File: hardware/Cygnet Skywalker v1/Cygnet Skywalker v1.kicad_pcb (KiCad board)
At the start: 2 copper layers, 85 parts, among them J3 BM04B-SRSS-TB(LF)(SN), J4 BM04B-SRSS-TB(LF)(SN), J5 BM04B-SRSS-TB(LF)(SN), J7 Conn_01x02, J8 Hirose DF11 02x06, SW1 SW_Push, SW2 SW_Push, U1 RP2350_60QFN_C42411118, U11 RM-VT01-A Readout Module, U12 INA260, U13 INA260, U14 TLV1704, U15 REF200AU, U2 W25Q128JVS, U3 INA260, U5 MCP9808_MSOP, U6 VT01, U7 NCP1117-3.3_SOT223, Y1 ABM8-272-T3

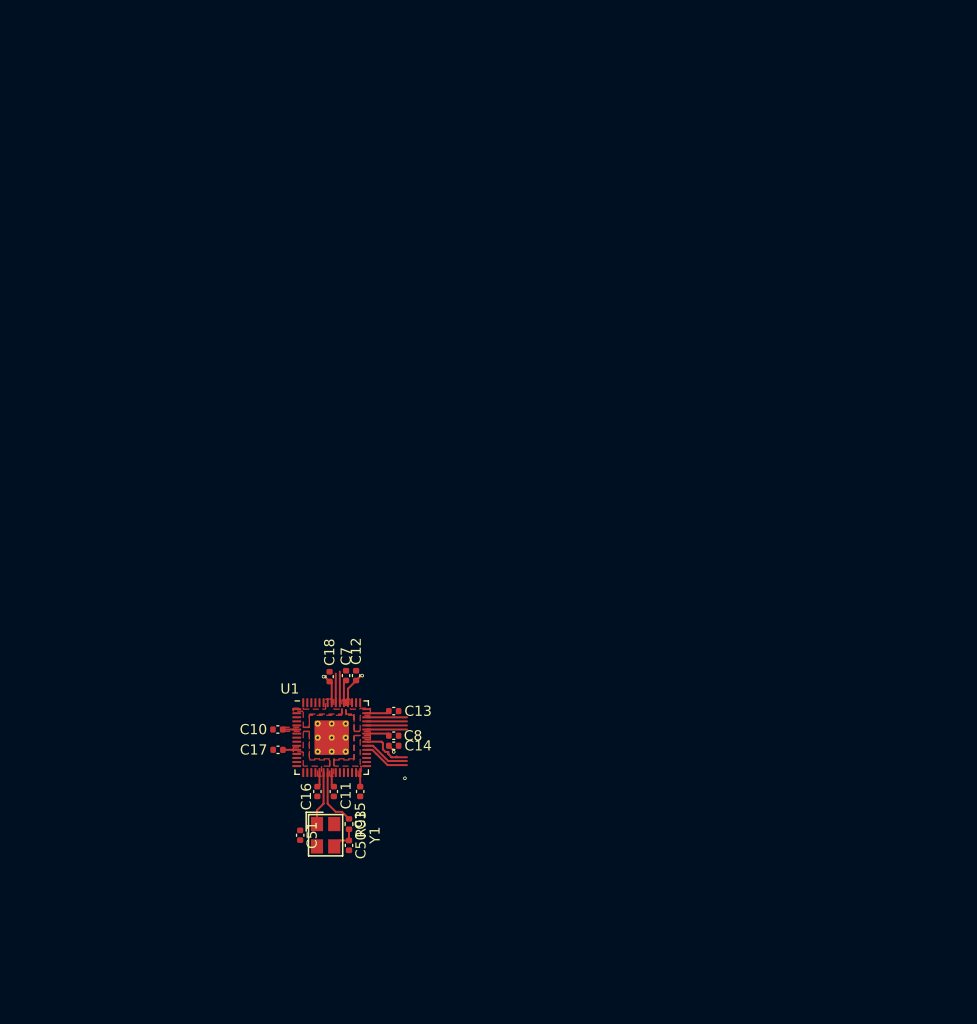
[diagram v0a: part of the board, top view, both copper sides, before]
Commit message: added edge cut for PCB
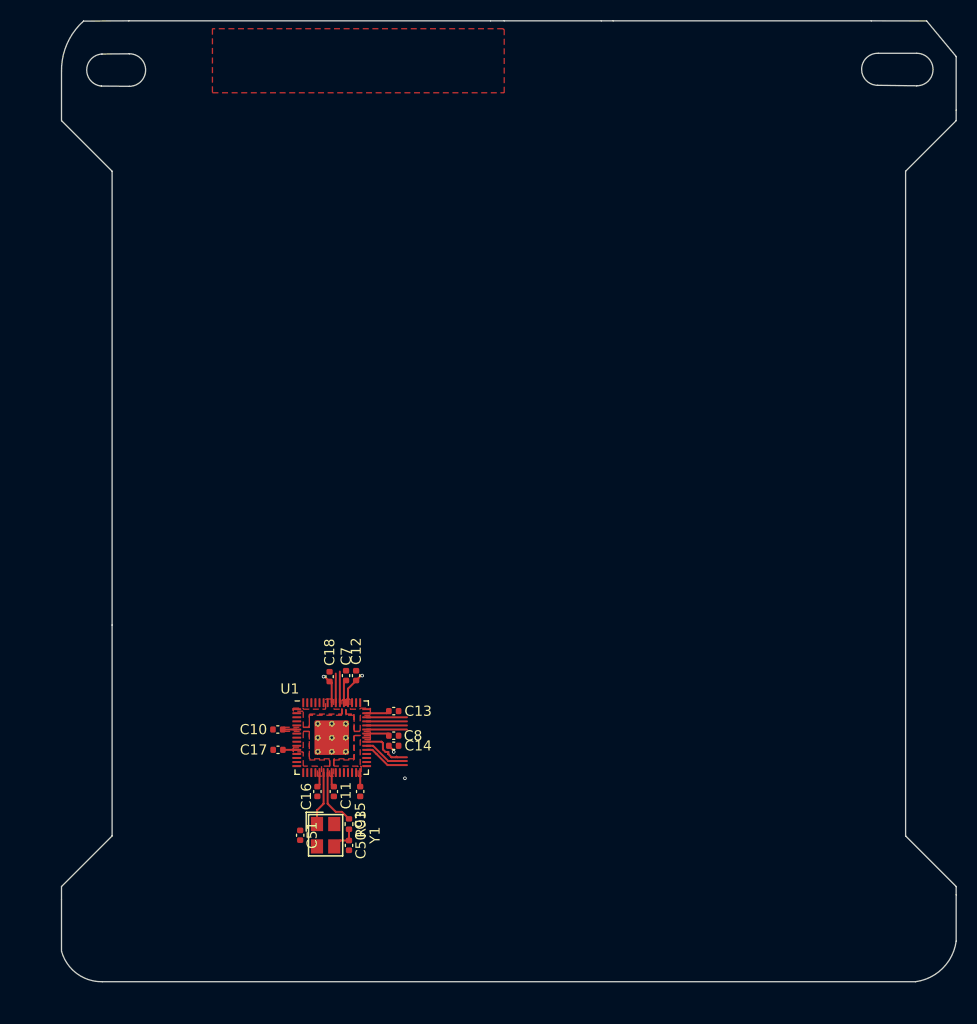
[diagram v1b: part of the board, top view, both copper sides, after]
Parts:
- added G***: LOGO, LOGO, F.Cu at (200.9, 46.0)
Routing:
- added copper zone on F.Cu, net PAYLOAD_PWR
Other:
- board outline added: 88 x 94.5 mm
- board text added: "${REFERENCE}"

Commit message: brought over changes made on max branch
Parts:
- removed C20: 100n, Capacitor_SMD:C_0402_1005Metric
- removed C21: 1u, Capacitor_SMD:C_0402_1005Metric
- removed C22, C23: 10u, Capacitor_SMD:C_0805_2012Metric
- removed C33: 10u, Capacitor_SMD:C_0402_1005Metric
- removed U15: REF200AU, Package_SO:SOIC-8_3.9x4.9mm_P1.27mm
- removed U7: NCP1117-3.3_SOT223, Package_TO_SOT_SMD:SOT-223-3_TabPin2
- added D14: NSR0320, Diode_SMD:D_SOD-323F, F.Cu at (139.1, 120.5)
- added U17: LM234Z-6, Package_TO_SOT_THT:TO-92_Inline, F.Cu at (139.0, 114.5)
- C39: value 100n -> 1u
- moved G*** 26.5 mm to (201.1, 72.4)
- moved U11 25.9 mm to (129.0, 61.3)
- moved C13 13.3 mm to (213.4, 120.1)
- moved C14 13.3 mm to (213.4, 123.5)
- moved C17 13.3 mm to (202.0, 123.9)
- moved C18 13.3 mm to (207.1, 116.7)
- moved C7 13.3 mm to (208.7, 116.6)
- moved C8 13.3 mm to (213.4, 122.5)
- moved U1 13.3 mm to (207.3, 122.7)
- moved C50 13.3 mm to (209.0, 133.3)
- moved C51 13.3 mm to (204.2, 132.3)
- moved Y1 13.3 mm to (206.7, 132.3)
- moved C10 13.3 mm to (202.0, 121.9)
- moved C11 13.3 mm to (207.5, 128.0)
- moved C12 13.3 mm to (209.7, 116.6)
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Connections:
- R16 pad 1: /CubeSat's Best Friend/WDT-VIN -> +5V
- R30 pad 1: /CubeSat's Best Friend/WDT-VIN -> +5V
- R36 pad 2: /CubeSat's Best Friend/WDT-VIN -> +5V
- SW1 pad 2: /RP2350/QSPI_SS -> Net-(R26-Pad2)
- U14 pad 3: /CubeSat's Best Friend/WDT-VIN -> +5V
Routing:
- added copper zone on F.Cu, net (none)
- removed copper zone on F.Cu, net PAYLOAD_PWR
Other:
- board text removed: "${REFERENCE}"

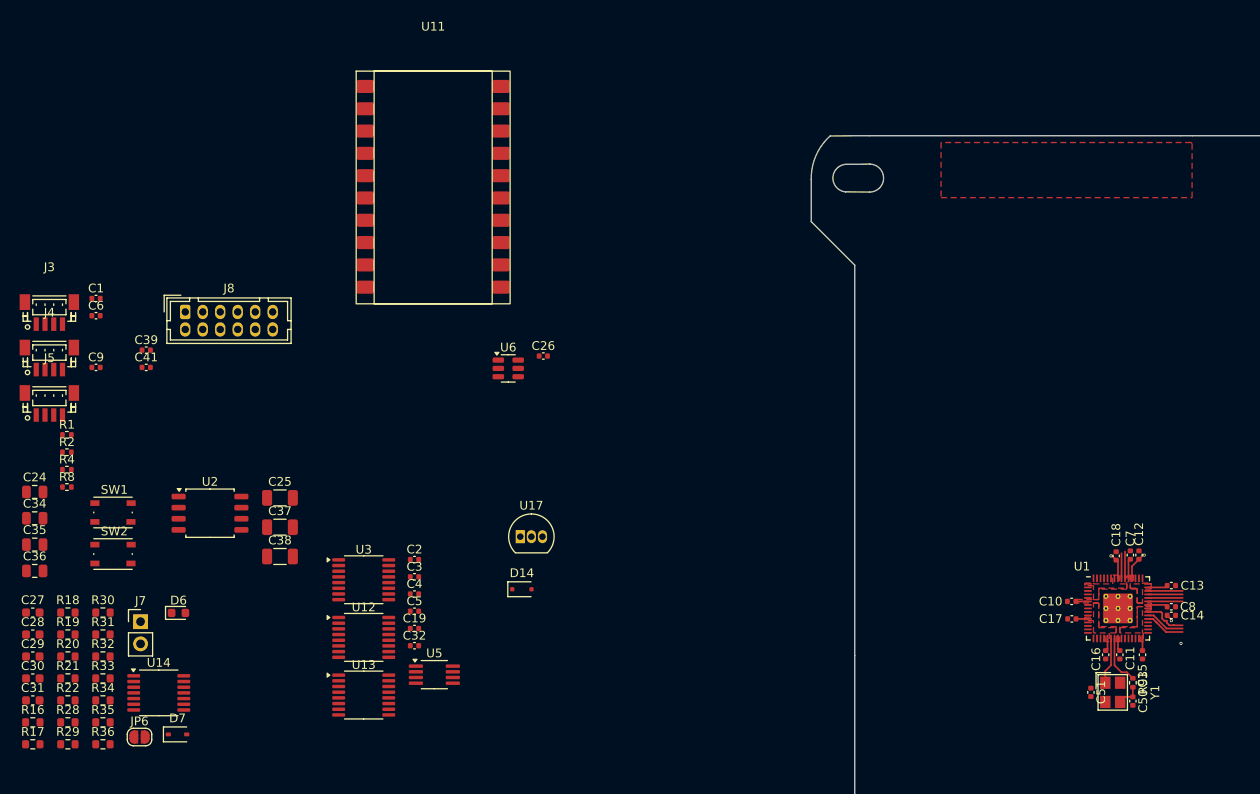
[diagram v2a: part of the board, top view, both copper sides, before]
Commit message: schematic changes
-replaced custom circuitry with radfet readout modules
-cleaned up sensor schematic page
-changed temp sensor
-added more missing footprints
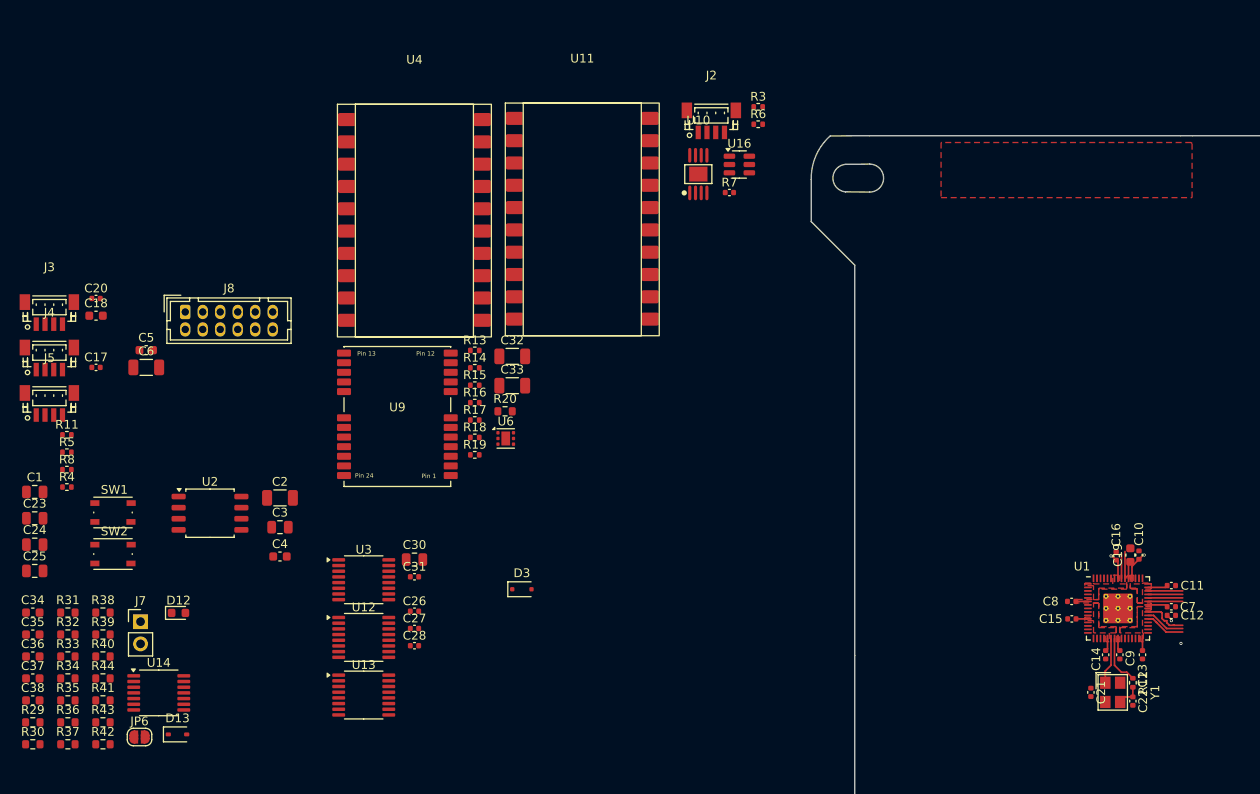
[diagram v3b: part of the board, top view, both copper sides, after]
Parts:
- removed the C26 at (141.6, 93.8)
- removed the C4 at (126.9, 121.1)
- removed U17: LM234Z-6, Package_TO_SOT_THT:TO-92_Inline
- removed U5: MCP9808_MSOP, Package_SO:MSOP-8_3x3mm_P0.65mm
- added C32: 10u, Capacitor_SMD:C_1206_3216Metric, F.Cu at (138.0, 93.9)
- added C33: 10u, Capacitor_SMD:C_1206_3216Metric, F.Cu at (138.0, 97.2)
- added J2: BM04B-SRSS-TB(LF)(SN), Skywalkerfeet:BM04B-SRSS-TB(LF)(SN), F.Cu at (160.8, 67.0)
- added R13: 1k, Resistor_SMD:R_0402_1005Metric, F.Cu at (133.8, 93.2)
- added R14: 10k, Resistor_SMD:R_0402_1005Metric, F.Cu at (133.8, 95.2)
- added R15: 10k, Resistor_SMD:R_0402_1005Metric, F.Cu at (133.8, 97.2)
- added R16: 10k, Resistor_SMD:R_0402_1005Metric, F.Cu at (133.8, 99.2)
- added R17: 10k, Resistor_SMD:R_0402_1005Metric, F.Cu at (133.8, 101.2)
- added R18: 10k, Resistor_SMD:R_0402_1005Metric, F.Cu at (133.8, 103.2)
- added R19: 6.8k, Resistor_SMD:R_0402_1005Metric, F.Cu at (133.8, 105.1)
- added R20: 20k, Resistor_SMD:R_0603_1608Metric, F.Cu at (137.2, 100.2)
- added R3: 33, Resistor_SMD:R_0402_1005Metric, F.Cu at (166.2, 65.4)
- added R6: 1k, Resistor_SMD:R_0402_1005Metric, F.Cu at (166.2, 67.3)
- added R7: 10k, Capacitor_SMD:C_0402_1005Metric, F.Cu at (162.9, 75.2)
- added U10: TLV76733DGNR, Skywalkerfeet:TLV76733DGNR, F.Cu at (159.3, 73.0)
- added U16: TLV61048, Package_TO_SOT_SMD:SOT-23-6, F.Cu at (164.0, 72.0)
- added U4: RM-VT01-A Readout Module, Skywalkerfeet:RM-VT01-A, F.Cu at (126.9, 65.1)
- added U9: Skytraq Orion B16 GPS, Skywalkerfeet:Skytraq Orion B16 GPS, F.Cu at (124.9, 99.7)
- C18: renamed from C6; footprint Capacitor_SMD:C_0402_1005Metric -> Capacitor_SMD:C_0603_1608Metric
- C19: renamed from C7; footprint Capacitor_SMD:C_0402_1005Metric -> Capacitor_SMD:C_0603_1608Metric
- C3: renamed from C37; footprint Capacitor_SMD:C_1206_3216Metric -> Capacitor_SMD:C_0805_2012Metric
- C30: renamed from C2; footprint Capacitor_SMD:C_0402_1005Metric -> Capacitor_SMD:C_0805_2012Metric
- C4: renamed from C38; footprint Capacitor_SMD:C_1206_3216Metric -> Capacitor_SMD:C_0603_1608Metric
- C5: renamed from C39; footprint Capacitor_SMD:C_0402_1005Metric -> Capacitor_SMD:C_0603_1608Metric
- C6: renamed from C41; footprint Capacitor_SMD:C_0402_1005Metric -> Capacitor_SMD:C_1206_3216Metric
- U6: value VT01 -> TMP117xxDRV; footprint Package_TO_SOT_SMD:SOT-23-6 -> Package_SON:WSON-6-1EP_2x2mm_P0.65mm_EP1x1.6mm
- moved U11 17.4 mm to (146.1, 65.0)
- moved U6 8.02 mm to (137.3, 103.3)
- renumbered C24 to C1, C12 to C10, C13 to C11, C14 to C12, C15 to C13, C16 to C14, C17 to C15, C18 to C16, C9 to C17, C25 to C2, C1 to C20, C51 to C21, C50 to C22, C34 to C23, C35 to C24, C36 to C25, C5 to C26, C19 to C27, C32 to C28, C3 to C31, C27 to C34, C28 to C35, C29 to C36, C30 to C37, C31 to C38, C8 to C7, C10 to C8, C11 to C9, D6 to D12, D7 to D13, D14 to D3, R1 to R11, R93 to R12, R16 to R29, R17 to R30, R18 to R31, R19 to R32, R20 to R33, R21 to R34, R22 to R35, R28 to R36, R29 to R37, R30 to R38, R31 to R39, R8 to R4, R32 to R40, R34 to R41, R36 to R42, R35 to R43, R33 to R44, R2 to R5, R4 to R8
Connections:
- U1 pad 10: RADFET Sense CTRL -> unconnected-(U1-GPIO7-Pad10)
- U1 pad 12: RADFET Read CTRL -> unconnected-(U1-GPIO8-Pad12)
- U1 pad 8: RADFET R2 CTRL -> unconnected-(U1-GPIO5-Pad8)
- U1 pad 9: RADFET R1 CTRL -> unconnected-(U1-GPIO6-Pad9)
- U12 pad 5: unconnected-(U12-A0-Pad5) -> SDA1
- U3 pad 4: unconnected-(U3-A1-Pad4) -> GND
- U3 pad 5: unconnected-(U3-A0-Pad5) -> +3.3V
- U6 pad 1: Net-(R27-Pad2) -> SCL1
- U6 pad 2: RADFET Vo -> GND
- U6 pad 3: Net-(Q4-D) -> unconnected-(U6-ALERT-Pad3)
- U6 pad 4: Net-(Q5-D) -> GND
- U6 pad 5: Net-(Q4-D) -> +3.3V
- U6 pad 6: Net-(Q5-D) -> SDA1

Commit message: carried over cygnet skywalker v1 from max-layout
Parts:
- removed the G*** at (201.1, 72.4)
- removed JP6: SolderJumper_2_Open, Jumper:SolderJumper-2_P1.3mm_Open_RoundedPad1.0x1.5mm
- removed R42, R44: 100k, Resistor_SMD:R_0603_1608Metric
- removed R43: 4.7M, Resistor_SMD:R_0603_1608Metric
- removed U16: TLV61048, Package_TO_SOT_SMD:SOT-23-6
- added C29: 100n, Capacitor_SMD:C_0402_1005Metric, F.Cu at (223.2, 96.2)
- added C39: 10uF, Capacitor_SMD:C_0603_1608Metric, F.Cu at (250.7, 91.5)
- added C40: 10uF, Capacitor_SMD:C_0603_1608Metric, F.Cu at (249.2, 91.5)
- added C41: 10uF, Capacitor_SMD:C_0603_1608Metric, F.Cu at (244.0, 86.0)
- added C42: 10uF, Capacitor_SMD:C_0603_1608Metric, F.Cu at (244.0, 87.5)
- added C43: 10uF, Capacitor_SMD:C_0603_1608Metric, F.Cu at (252.8, 83.0)
- added D1: RED, LED_SMD:LED_0603_1608Metric, F.Cu at (199.6, 79.6)
- added D10: YELLOW, LED_SMD:LED_0603_1608Metric, F.Cu at (214.9, 157.4)
- added D11: B120AF-13, Skywalkerfeet:B120AF-13, F.Cu at (209.7, 90.6)
- added D2: B120AF-13, Skywalkerfeet:B120AF-13, F.Cu at (194.8, 96.0)
- added D4: BLUE, LED_SMD:LED_0603_1608Metric, F.Cu at (193.4, 79.5)
- added D5: WHITE, LED_SMD:LED_0603_1608Metric, F.Cu at (190.1, 79.6)
- added D6: NSR0320, Diode_SMD:D_SOD-323F, F.Cu at (204.3, 114.7)
- added D7: RED, LED_SMD:LED_0603_1608Metric, F.Cu at (196.2, 137.4)
- added D8: RED, LED_SMD:LED_0603_1608Metric, F.Cu at (193.0, 137.4)
- added D9: YELLOW, LED_SMD:LED_0603_1608Metric, F.Cu at (218.1, 157.5)
- added G***: LOGO, LOGO, F.Cu at (208.0, 70.6)
- added G***: LOGO, 1my_footprints:cadence_cygnet_logo_placeholder, F.Cu at (227.7, 70.9)
- added G***: LOGO, LOGO, B.Cu at (249.4, 111.7)
- added H1: MountingHole, MountingHole:MountingHole_3.2mm_M3_DIN965_Pad, F.Cu at (184.3, 156.9)
- added H2: MountingHole, MountingHole:MountingHole_3.2mm_M3_DIN965_Pad, F.Cu at (264.3, 156.9)
- added J1: USB_B_Micro, Skywalkerfeet:MICRO-USB-SMD_10118194-0001LF, F.Cu at (188.3, 99.8)
- added J10: BM04B-SRSS-TB(LF)(SN), Skywalkerfeet:BM04B-SRSS-TB(LF)(SN), F.Cu at (203.2, 136.4)
- added J11: Conn_Coaxial, Skywalkerfeet:SMA-TH_132134, F.Cu at (192.0, 144.1)
- added J12: Conn_01x02, Connector_PinHeader_2.54mm:PinHeader_1x02_P2.54mm_Vertical, F.Cu at (240.7, 91.8)
- added J6: BM04B-SRSS-TB(LF)(SN), Skywalkerfeet:BM04B-SRSS-TB(LF)(SN), F.Cu at (208.1, 104.0)
- added J9: BM04B-SRSS-TB(LF)(SN), Skywalkerfeet:BM04B-SRSS-TB(LF)(SN), F.Cu at (234.2, 148.7)
- added JP1: SolderJumper_2_Open, Jumper:SolderJumper-2_P1.3mm_Open_RoundedPad1.0x1.5mm, F.Cu at (242.8, 79.9)
- added L1: 3.3u, Skywalkerfeet:L_pol_2016, F.Cu at (221.9, 113.9)
- added L2: 2.2uH, Inductor_SMD:L_Coilcraft_XxL4020, F.Cu at (194.3, 104.8)
- added L3: 4.7uH, Skywalkerfeet:SWPA5040S4R7NT, F.Cu at (207.0, 84.5)
- added R1: 10k, Resistor_SMD:R_0402_1005Metric, F.Cu at (205.4, 108.8)
- added R10: 33, Resistor_SMD:R_0402_1005Metric, F.Cu at (224.3, 113.6)
- added R2: 1k, Resistor_SMD:R_0402_1005Metric, F.Cu at (221.7, 129.0)
- added R21: 1.5M, Resistor_SMD:R_0603_1608Metric, F.Cu at (214.0, 86.2)
- added R22: 107k, Resistor_SMD:R_0603_1608Metric, F.Cu at (214.0, 83.2)
- added R23: 4.7k, Resistor_SMD:R_0402_1005Metric, F.Cu at (227.7, 123.5)
- added R24: 4.7k, Resistor_SMD:R_0402_1005Metric, F.Cu at (229.2, 125.0)
- added R25: 10k, Resistor_SMD:R_0603_1608Metric, F.Cu at (252.2, 80.3)
- added R26: 10k, Resistor_SMD:R_0603_1608Metric, F.Cu at (252.8, 84.5)
- added R27: 10k, Resistor_SMD:R_0603_1608Metric, F.Cu at (252.8, 89.0)
- added R28: 3.0k, Resistor_SMD:R_0603_1608Metric, F.Cu at (252.8, 87.5)
- added R9: 1k, Resistor_SMD:R_0402_1005Metric, F.Cu at (206.5, 116.5)
- added TP1: 3.3V Testpoint, Skywalkerfeet:Keystone5001_Testpoint, F.Cu at (203.9, 77.8)
- added TP10: GND, Skywalkerfeet:Keystone5001_Testpoint, F.Cu at (227.4, 93.9)
- added TP2: Module1 Vo, Skywalkerfeet:Keystone5001_Testpoint, F.Cu at (234.6, 121.0)
- added TP3: 5V Testpoint, Skywalkerfeet:Keystone5001_Testpoint, F.Cu at (211.5, 77.8)
- added TP4: Module2 Vo, Skywalkerfeet:Keystone5001_Testpoint, F.Cu at (231.8, 116.5)
- added TP5: 12V Testpoint, Skywalkerfeet:Keystone5001_Testpoint, F.Cu at (219.3, 77.9)
- added TP6: GPS 1PPS, Skywalkerfeet:Keystone5001_Testpoint, F.Cu at (211.1, 139.7)
- added TP7: 7V Testpoint, Skywalkerfeet:Keystone5001_Testpoint, F.Cu at (226.5, 78.0)
- added TP8: GND, Skywalkerfeet:Keystone5001_Testpoint, F.Cu at (227.4, 85.0)
- added TP9: GND, Skywalkerfeet:Keystone5001_Testpoint, F.Cu at (227.3, 89.3)
- added U15: TLV1704, Package_SO:TSSOP-14_4.4x5mm_P0.65mm, F.Cu at (248.4, 85.8)
- added U5: TLV61048, Package_TO_SOT_SMD:SOT-23-6, F.Cu at (211.5, 84.3)
- added U7: INA260, Package_SO:TSSOP-16_4.4x5mm_P0.65mm, F.Cu at (202.0, 91.9)
- added U8: INA260, Package_SO:TSSOP-16_4.4x5mm_P0.65mm, F.Cu at (195.4, 127.2)
- C1: value 10u -> 15p; footprint Capacitor_SMD:C_0805_2012Metric -> Capacitor_SMD:C_0402_1005Metric
- C10, C11: value 100n -> 4.7u
- C12: value 100n -> 3.3nF; footprint Capacitor_SMD:C_0402_1005Metric -> Capacitor_SMD:C_0603_1608Metric
- C14: value 100n -> 22u; footprint Capacitor_SMD:C_0402_1005Metric -> Capacitor_SMD:C_1206_3216Metric
- C16, C7: value 100n -> 1u; footprint Capacitor_SMD:C_0402_1005Metric -> Capacitor_SMD:C_0603_1608Metric
- C17, C8: value 4.7u -> 100n
- C18, C19: value 4.7u -> 100n; footprint Capacitor_SMD:C_0603_1608Metric -> Capacitor_SMD:C_0402_1005Metric
- C2: value 22u -> 15p; footprint Capacitor_SMD:C_1206_3216Metric -> Capacitor_SMD:C_0402_1005Metric
- C21: value 15p -> 100n
- C22: value 15p -> 10u; footprint Capacitor_SMD:C_0402_1005Metric -> Capacitor_SMD:C_1206_3216Metric
- C23, C30: value 10u -> 100n; footprint Capacitor_SMD:C_0805_2012Metric -> Capacitor_SMD:C_0402_1005Metric
- C26, C27, C28, C9: value 100n -> 10u; footprint Capacitor_SMD:C_0402_1005Metric -> Capacitor_SMD:C_0805_2012Metric
- C3: value 2.2u -> 1u; footprint Capacitor_SMD:C_0805_2012Metric -> Capacitor_SMD:C_0603_1608Metric
- C33: value 10u -> 100n; footprint Capacitor_SMD:C_1206_3216Metric -> Capacitor_SMD:C_0402_1005Metric
- C34, C37: value 10uF -> 100n; footprint Capacitor_SMD:C_0603_1608Metric -> Capacitor_SMD:C_0402_1005Metric
- C35: value 10uF -> 10u; footprint Capacitor_SMD:C_0603_1608Metric -> Capacitor_SMD:C_1206_3216Metric
- C36: value 10uF -> 10u; footprint Capacitor_SMD:C_0603_1608Metric -> Capacitor_SMD:C_0805_2012Metric
- C38: value 10uF -> 2.7n
- C4: value 1u -> 100n; footprint Capacitor_SMD:C_0603_1608Metric -> Capacitor_SMD:C_0402_1005Metric
- C5: value 1u -> 4.7u; footprint Capacitor_SMD:C_0603_1608Metric -> Capacitor_SMD:C_0402_1005Metric
- C6: value 10u -> 4.7u; footprint Capacitor_SMD:C_1206_3216Metric -> Capacitor_SMD:C_0402_1005Metric
- D3: value NSR0320 -> GREEN; footprint Diode_SMD:D_SOD-323F -> LED_SMD:LED_0603_1608Metric
- J2, J4: value BM04B-SRSS-TB(LF)(SN) -> Hirose DF11 02x06; footprint Skywalkerfeet:BM04B-SRSS-TB(LF)(SN) -> Connector_Hirose:Hirose_DF11-12DP-2DSA_2x06_P2.00mm_Vertical
- J3: value BM04B-SRSS-TB(LF)(SN) -> SWD Port; footprint Skywalkerfeet:BM04B-SRSS-TB(LF)(SN) -> Connector_PinHeader_1.27mm:PinHeader_2x02_P1.27mm_Vertical
- J7: value Conn_01x02 -> BM04B-SRSS-TB(LF)(SN); footprint Connector_PinHeader_2.54mm:PinHeader_1x02_P2.54mm_Vertical -> Skywalkerfeet:BM04B-SRSS-TB(LF)(SN)
- J8: value Hirose DF11 02x06 -> BM04B-SRSS-TB(LF)(SN); footprint Connector_Hirose:Hirose_DF11-12DP-2DSA_2x06_P2.00mm_Vertical -> Skywalkerfeet:BM04B-SRSS-TB(LF)(SN)
- R11: footprint Resistor_SMD:R_0402_1005Metric -> Capacitor_SMD:C_0402_1005Metric
- R12: value 1k -> 10k; footprint Resistor_SMD:R_0402_1005Metric -> Resistor_SMD:R_0603_1608Metric
- R13: value 1k -> 10k
- R14, R15, R16: footprint Resistor_SMD:R_0402_1005Metric -> Resistor_SMD:R_0603_1608Metric
- R17, R18: value 10k -> 27
- R19: value 6.8k -> 4.7k
- R20: value 20k -> 4.7k; footprint Resistor_SMD:R_0603_1608Metric -> Resistor_SMD:R_0402_1005Metric
- R29, R30: value 10k -> 3.0k
- R3: value 33 -> 220; footprint Resistor_SMD:R_0402_1005Metric -> Resistor_SMD:R_0603_1608Metric
- R32: value 3.0k -> 10k
- R33: value 3.0k -> 1k
- R34: value 3.0k -> 100k
- R35: value 10k -> 1k
- R36: value 10k -> 100k
- R37: value 1k -> 100k
- R39: value 1k -> 4.7M
- R4: value 27 -> 470; footprint Resistor_SMD:R_0402_1005Metric -> Resistor_SMD:R_0603_1608Metric
- R41: value 100k -> 4.7k; footprint Resistor_SMD:R_0603_1608Metric -> Resistor_SMD:R_0402_1005Metric
- R5: value 27 -> 10k
- R6: value 1k -> 1.47k; footprint Resistor_SMD:R_0402_1005Metric -> Resistor_SMD:R_0603_1608Metric
- R7: value 10k -> 1k; footprint Capacitor_SMD:C_0402_1005Metric -> Resistor_SMD:R_0402_1005Metric
- R8: value 1k -> 330; footprint Resistor_SMD:R_0402_1005Metric -> Resistor_SMD:R_0603_1608Metric
- SW1, SW2: footprint Button_Switch_SMD:SW_Push_1P1T_NO_Vertical_Wuerth_434133025816 -> Skywalkerfeet:KEY-SMD_KMR2XXGXXX
- U1: value RP2350_60QFN_C42411118 -> W25Q128JVS; footprint Skywalkerfeet:RP2350-QFN-60-1EP_7x7_P0.4mm_EP3.4x3.4mm_ThermalVias -> Package_SO:SOIC-8_5.3x5.3mm_P1.27mm
- U10: value TLV76733DGNR -> INA260; footprint Skywalkerfeet:TLV76733DGNR -> Package_SO:TSSOP-16_4.4x5mm_P0.65mm
- U12: value INA260 -> RM-VT01-A Readout Module; footprint Package_SO:TSSOP-16_4.4x5mm_P0.65mm -> Skywalkerfeet:RM-VT01-A
- U13: value INA260 -> Skytraq Orion B16 GPS; footprint Package_SO:TSSOP-16_4.4x5mm_P0.65mm -> Skywalkerfeet:Skytraq Orion B16 GPS
- U14: value TLV1704 -> TPS22992; footprint Package_SO:TSSOP-14_4.4x5mm_P0.65mm -> Skywalkerfeet:TPS22992
- U2: value W25Q128JVS -> TLV76733DGNR; footprint Package_SO:SOIC-8_5.3x5.3mm_P1.27mm -> Skywalkerfeet:TLV76733DGNR
- U3: value INA260 -> TPS62142; footprint Package_SO:TSSOP-16_4.4x5mm_P0.65mm -> Package_DFN_QFN:VQFN-16-1EP_3x3mm_P0.5mm_EP1.68x1.68mm_ThermalVias
- U4: value RM-VT01-A Readout Module -> RP2350_60QFN_C42411118; footprint Skywalkerfeet:RM-VT01-A -> Skywalkerfeet:RP2350-QFN-60-1EP_7x7_P0.4mm_EP3.4x3.4mm_ThermalVias
- U6: value TMP117xxDRV -> INA260; footprint Package_SON:WSON-6-1EP_2x2mm_P0.65mm_EP1x1.6mm -> Package_SO:TSSOP-16_4.4x5mm_P0.65mm
- U9: value Skytraq Orion B16 GPS -> TMP117xxDRV; footprint Skywalkerfeet:Skytraq Orion B16 GPS -> Package_SON:WSON-6-1EP_2x2mm_P0.65mm_EP1x1.6mm
- moved R29 176.7 mm to (252.8, 86.0)
- moved R30 175.3 mm to (252.2, 91.5), turned to 90 degrees
- moved R36 171.2 mm to (249.2, 80.3), turned to 90 degrees
- moved R39 165.8 mm to (250.7, 80.3), turned to -90 degrees
- moved R37 165.7 mm to (244.0, 84.5)
- moved R32 164.1 mm to (247.7, 91.5), turned to 90 degrees
- moved R34 163.7 mm to (246.2, 91.5), turned to -90 degrees
- moved R35 162.9 mm to (244.0, 89.0), turned to 180 degrees
- moved R38 162.2 mm to (247.7, 80.3), turned to 90 degrees
- moved R40 162.2 mm to (246.2, 80.3), turned to 90 degrees
- moved R33 161.7 mm to (244.7, 91.5), turned to -90 degrees
- moved R31 159.1 mm to (243.2, 91.5), turned to 90 degrees
- moved D12 157.0 mm to (253.7, 91.5), turned to 90 degrees
- moved C35 155.0 mm to (235.6, 97.0), turned to 180 degrees
- moved D13 154.0 mm to (243.9, 82.8), turned to 180 degrees
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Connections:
- C1 pad 1: PAYLOAD_BATT -> /RP2350/XIN
- C10 pad 1: +3.3V -> /RP2350/VREG_AVDD
- C11 pad 1: +3.3V -> +1V1
- C12 pad 1: +3.3V -> Net-(U3-SS/TR)
- C13 pad 1: +3.3V -> +1V1
- C14 pad 1: +3.3V -> PAYLOAD_PWR Test
- C17 pad 1: /RP2350/VREG_AVDD -> +3.3V
- C19 pad 1: +1V1 -> +3.3V
- C2 pad 1: +5V -> Net-(C2-Pad1)
- C21 pad 1: /RP2350/XIN -> +3.3V
- C22 pad 1: Net-(C22-Pad1) -> RADFET_PWR
- C23 pad 1: +5V -> +3.3V
- C3 pad 1: +3.3V -> +5V
- C33 pad 1: +12V -> +3.3V
- C34 pad 1: PET DOG -> +3.3V
- C34 pad 2: Net-(C34-Pad2) -> GND
- C35 pad 1: GND -> +12V
- C35 pad 2: Net-(U14B-+) -> GND
- C36 pad 1: GND -> GPS_PWR_SW_OUT
- C36 pad 2: WDT_DISABLE -> GND
- C37 pad 1: GND -> GPS_PWR_SW_OUT
- C37 pad 2: WDT_DISABLE -> GND
- C38 pad 1: GND -> Net-(U14-CT)
- C38 pad 2: Net-(U14D--) -> GND
- C4 pad 1: Net-(D1-K) -> +3.3V
- C5 pad 1: +5V -> +3.3V
- C6 pad 1: +12V -> +1V1
- C7 pad 1: +1V1 -> PAYLOAD_PWR Test
- C9 pad 1: +1V1 -> PAYLOAD_BATT_OUT
- D13 pad 1: Net-(U14D-+) -> Net-(U15D-+)
- D3 pad 1: Net-(D3-K) -> GND
- D3 pad 2: /RP2350/QSPI_SS -> Net-(D3-A)
- J2 pad 1: GND -> +3.3V
- J2 pad 2: RP2350 SWCLK -> GND
- J2 pad 3: RP2350 SWD -> +3.3V
- J3 pad 1: GND -> RP2350 Reset
- J3 pad 2: USB_D- -> RP2350 SWCLK
- J3 pad 3: USB_D+ -> GND
- J3 pad 4: GND -> RP2350 SWD
- J4 pad 1: GND -> PAYLOAD_PWR
- J4 pad 2: SCL0 -> PAYLOAD_PWR
- J4 pad 3: SDA0 -> GND
- J5 pad 2: SCL1 -> RP2350 SWD
- J5 pad 3: SDA1 -> RP2350 SWCLK
- J7 pad 1: WDT_DISABLE -> GND
- J7 pad 2: GND -> UART0 Tx
- J8 pad 1: PAYLOAD_PWR Test -> GND
- J8 pad 2: PAYLOAD_PWR Test -> SCL1
- J8 pad 3: GND -> SDA1
- R11 pad 2: /RP2350/QSPI_SS -> RP2350 Reset
- R12 pad 1: /RP2350/XOUT -> UART0 Tx
- R12 pad 2: Net-(C22-Pad1) -> Net-(D7-A)
- R13 pad 1: GPS Reset -> PAYLOAD_BATT_OUT
- R13 pad 2: GND -> DOG Bite
- R15 pad 1: UART0 Tx -> UART1 Tx
- R17 pad 1: UART1 Tx -> USB_D+
- R17 pad 2: Net-(D7-A) -> Net-(U4-USB_DP)
- R18 pad 1: +5V -> Net-(U4-USB_DM)
- R18 pad 2: Net-(D8-A) (its old number) -> USB_D-
- R19 pad 2: Net-(D9-A) (its old number) -> SCL0
- R20 pad 1: +12V -> +3.3V
- R20 pad 2: Net-(D10-A) (its old number) -> SDA0
- R29 pad 1: +5V -> /CubeSat's Best Friend/WDT-VP
- R29 pad 2: Net-(R29-Pad2) -> GND
- R3 pad 2: /RP2350/VREG_AVDD -> Net-(D1-A)
- R30 pad 1: Net-(R29-Pad2) -> PET DOG
- R30 pad 2: Net-(U14D--) -> Net-(D12-A)
- R31 pad 1: Net-(U14D--) -> Net-(C39-Pad2)
- R31 pad 2: Net-(U14B--) -> GND
- R32 pad 1: Net-(U14B--) -> Net-(C39-Pad2)
- R32 pad 2: /CubeSat's Best Friend/WDT-VP -> Net-(U15A--)
- R33 pad 1: /CubeSat's Best Friend/WDT-VP -> Net-(R33-Pad1)
- R33 pad 2: GND -> Net-(U15B-+)
- R34 pad 1: PET DOG -> +3.3V
- R34 pad 2: Net-(D12-A) -> Net-(U15B-+)
- R35 pad 1: Net-(C34-Pad2) -> Net-(R35-Pad1)
- R35 pad 2: GND -> WDT_DISABLE
- R36 pad 1: Net-(C34-Pad2) -> Net-(U15C-+)
- R36 pad 2: Net-(U14A--) -> Net-(R25-Pad2)
- R37 pad 1: Net-(R37-Pad1) -> Net-(D13-Pad2)
- R37 pad 2: Net-(U14B-+) -> WDT_DISABLE
- R38 pad 1: +5V -> Net-(U15C-+)
- R38 pad 2: Net-(U14B-+) -> Net-(U15D-+)
- R39 pad 1: Net-(R39-Pad1) -> Net-(U15D-+)
- R4 pad 1: USB D+ -> +5V
- R4 pad 2: Net-(U1-USB_DP) -> Net-(D3-A)
- R40 pad 1: Net-(U14C-+) -> Net-(U15D-+)
- R40 pad 2: Net-(R29-Pad2) -> +3.3V
- R41 pad 1: Net-(U14C-+) -> GPS Reset
- R41 pad 2: Net-(U14D-+) -> GND
- R5 pad 1: Net-(U1-USB_DM) -> +5V
- R5 pad 2: USB D- -> DOG Bite
- R6 pad 1: Net-(D3-K) -> +12V
- R6 pad 2: Net-(R6-Pad2) -> Net-(D4-A)
- R7 pad 1: +3.3V -> Net-(R7-Pad1)
- R7 pad 2: Net-(U1-RUN) -> GND
- R8 pad 1: Net-(R8-Pad1) -> PAYLOAD_BATT_OUT
- R8 pad 2: GND -> Net-(D5-A)
- SW1 pad 2: Net-(R6-Pad2) -> (no net)
- SW2 pad 1: Net-(R8-Pad1) -> Net-(R7-Pad1)
- SW2 pad 2: Net-(U1-RUN) -> (no net)
- U1 pad 1: +3.3V -> /RP2350/QSPI_SS
- U1 pad 2: UART0 Tx -> /RP2350/QSPI_SD1
- U1 pad 3: UART0 Rx -> /RP2350/QSPI_SD2
- U1 pad 4: Module R1 CTRL -> GND
- U1 pad 5: Module Enable CTRL -> /RP2350/QSPI_SD0
- U1 pad 6: +1V1 -> /RP2350/QSPI_SCLK
- U1 pad 7: Module R2 CTRL -> /RP2350/QSPI_SD3
- U1 pad 8: unconnected-(U1-GPIO5-Pad8) -> +3.3V
- U10 pad 3: unconnected-(U10-NC-Pad3) -> +3.3V
- U10 pad 4: GND -> SDA1
- U10 pad 5: DOG Bite -> SDA1
- U10 pad 8: Net-(D1-K) -> SDA1
- U10 pad 9: GND -> SCL1
- U11 pad 4: Module R2 CTRL -> Module1 R2 CTRL
- U11 pad 5: Module Enable CTRL -> Module1 Enable CTRL
- U11 pad 6: Module R1 CTRL -> Module1 R1 CTRL
- U11 pad 9: Module Vo -> Module1 Vo
- U12 pad 1: PAYLOAD_BATT Test -> +12V
- U12 pad 10: +3.3V -> (no net)
- U12 pad 11: GND -> (no net)
- U12 pad 12: PAYLOAD_BATT Test -> (no net)
- U12 pad 13: unconnected-(U12-NC-Pad13) -> (no net)
- U12 pad 14: PAYLOAD_BATT -> (no net)
- U12 pad 15: PAYLOAD_BATT -> (no net)
- U12 pad 16: PAYLOAD_BATT -> (no net)
- U12 pad 2: PAYLOAD_BATT Test -> GND
- U12 pad 3: PAYLOAD_BATT Test -> GND
- U12 pad 4: GND -> Module2 R2 CTRL
- U12 pad 5: SDA1 -> Module2 Enable CTRL
- U12 pad 6: GND -> Module2 R1 CTRL
- U12 pad 7: unconnected-(U12-ALERT-Pad7) -> (no net)
- U12 pad 8: SDA1 -> (no net)
- U12 pad 9: SCL1 -> Module2 Vo
- U13 pad 1: USB PWR Monitor -> unconnected-(U13-BOOT_SEL-Pad1)
- U13 pad 10: +3.3V -> GND
- U13 pad 11: GND -> Net-(J11-In)
- U13 pad 12: USB PWR Monitor -> GND
- U13 pad 13: unconnected-(U13-NC-Pad13) -> GND
- U13 pad 14: VBUS -> unconnected-(U13-SPI_MOSI-Pad14)
- U13 pad 15: VBUS -> (no net)
- U13 pad 16: VBUS -> unconnected-(U13-SPI_CLK-Pad16)
- U13 pad 2: USB PWR Monitor -> unconnected-(U13-SPI_MISO-Pad2)
- U13 pad 3: USB PWR Monitor -> GPS 1PPS
- U13 pad 4: GND -> (no net)
- U13 pad 5: GND -> (no net)
- U13 pad 6: GND -> (no net)
- U13 pad 7: unconnected-(U13-ALERT-Pad7) -> (no net)
- U13 pad 8: SDA1 -> GPS Reset
- U13 pad 9: SCL1 -> unconnected-(U13-SPI_CSN-Pad9)
- U14 pad 1: Net-(R39-Pad1) -> +3.3V
- U14 pad 2: Net-(R37-Pad1) -> GPS_PWR
- U14 pad 3: +5V -> GPS Power Good
- U14 pad 4: Net-(U14A--) -> GND
- U14 pad 5: /CubeSat's Best Friend/WDT-VP -> GPS Enable
- U14 pad 6: Net-(U14B--) -> Net-(U14-CT)
- U14 pad 7: Net-(U14B-+) -> GPS_PWR_SW_OUT
- U14 pad 8: WDT_DISABLE -> GPS_PWR_SW_OUT
- U2 pad 1: /RP2350/QSPI_SS -> PAYLOAD_PWR Test
- U2 pad 2: /RP2350/QSPI_SD1 -> PAYLOAD_PWR Test
- U2 pad 3: /RP2350/QSPI_SD2 -> unconnected-(U2-NC-Pad3)
- U2 pad 5: /RP2350/QSPI_SD0 -> DOG Bite
- U2 pad 6: /RP2350/QSPI_SCLK -> GND
- U2 pad 7: /RP2350/QSPI_SD3 -> unconnected-(U2-NC-Pad7)
- U2 pad 8: +3.3V -> +5V
- U3 pad 1: PAYLOAD_PWR Test -> Net-(L2-Pad1)
- U3 pad 10: +3.3V -> PAYLOAD_BATT_OUT
- U3 pad 11: GND -> PAYLOAD_BATT_OUT
- U3 pad 12: PAYLOAD_PWR Test -> PAYLOAD_BATT_OUT
- U3 pad 13: unconnected-(U3-NC-Pad13) -> DOG Bite
- U3 pad 14: +3.3V -> PAYLOAD_PWR Test
- U3 pad 15: +3.3V -> GND
- U3 pad 16: +3.3V -> GND
- U3 pad 2: PAYLOAD_PWR Test -> Net-(L2-Pad1)
- U3 pad 3: PAYLOAD_PWR Test -> Net-(L2-Pad1)
- U3 pad 5: +3.3V -> GND
- U3 pad 7: unconnected-(U3-ALERT-Pad7) -> GND
- U3 pad 8: SDA1 -> GND
- U3 pad 9: SCL1 -> Net-(U3-SS/TR)
- U4 pad 1: +12V -> +3.3V
- U4 pad 10: (no net) -> Module2 R2 CTRL
- U4 pad 11: (no net) -> +3.3V
- U4 pad 12: (no net) -> UART1 Tx
- U4 pad 13: (no net) -> UART1 Rx
- U4 pad 14: (no net) -> unconnected-(U4-GPIO10-Pad14)
- U4 pad 15: (no net) -> GPS Reset
- U4 pad 16: (no net) -> GPS Power Good
- U4 pad 17: (no net) -> GPS Enable
- U4 pad 18: (no net) -> unconnected-(U4-GPIO14-Pad18)
- U4 pad 19: (no net) -> GPIO15
- U4 pad 2: GND -> UART0 Tx
- U4 pad 20: (no net) -> +3.3V
- U4 pad 3: GND -> UART0 Rx
- U4 pad 4: Module R2 CTRL -> Module1 R1 CTRL
- U4 pad 5: Module Enable CTRL -> Module1 Enable CTRL
- U4 pad 6: Module R1 CTRL -> +1V1
- U4 pad 7: (no net) -> Module1 R2 CTRL
- U4 pad 8: (no net) -> Module2 R1 CTRL
- U4 pad 9: Module Vo -> Module2 Enable CTRL
- U6 pad 1: SCL1 -> RADFET_PWR
- U6 pad 2: GND -> RADFET_PWR
- U6 pad 3: unconnected-(U6-ALERT-Pad3) -> RADFET_PWR
- U6 pad 6: SDA1 -> GND
- U6 pad 7: (no net) -> unconnected-(U6-ALERT-Pad7)
- U9 pad 1: unconnected-(U9-BOOT_SEL-Pad1) -> SCL1
- U9 pad 2: unconnected-(U9-SPI_MISO-Pad2) -> GND
- U9 pad 3: GPS 1PPS -> unconnected-(U9-ALERT-Pad3)
- U9 pad 4: (no net) -> GND
- U9 pad 5: (no net) -> +3.3V
- U9 pad 6: (no net) -> SDA1
- Y1 pad 3: Net-(C22-Pad1) -> Net-(C2-Pad1)
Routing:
- net +12V: track 0.00 -> 134.1 mm
- net SDA1: track 0.00 -> 133.3 mm, vias 0 -> 9
- net SCL1: track 4.58 -> 135.6 mm, vias 0 -> 6
- net PAYLOAD_BATT_OUT: track 0.00 -> 114.0 mm, vias 0 -> 2
- net +3.3V: track 13.6 -> 108.4 mm, vias 3 -> 62
- net PET DOG: track 0.00 -> 90.8 mm, vias 0 -> 2
- net DOG Bite: track 0.00 -> 86.3 mm, vias 0 -> 3
- net Module1 R2 CTRL: track 0.00 -> 78.2 mm, vias 0 -> 2
- net Module1 Enable CTRL: track 0.00 -> 75.3 mm, vias 0 -> 2
- net Module1 R1 CTRL: track 0.00 -> 70.3 mm, vias 0 -> 2
- net GPS 1PPS: track 3.96 -> 65.8 mm, vias 0 -> 1
- net UART0 Rx: track 0.00 -> 56.1 mm, vias 0 -> 3
- net Module2 R1 CTRL: track 0.00 -> 55.6 mm, vias 0 -> 2
- net Module2 Enable CTRL: track 0.00 -> 55.2 mm, vias 0 -> 2
- net Module2 R2 CTRL: track 0.00 -> 54.8 mm, vias 0 -> 2
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- added copper zone on In2.Cu, net +3.3V
- added copper zone on B.Cu, net GND
- added copper zone on F.Cu, net GND
- added copper zone on In1.Cu, net GND
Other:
- outline, holes or cut-outs redrawn
- copper layers 2 -> 4
- board text added: "12V"
- board text added: "3.3V"
- board text added: "5V"
- board text added: "7V"
- board text added: "CYGNET RADFET Payload Board by William Hsu & Max Gross With Michael Pham's Stamp of Approval!"
- board text added: "Cygnet Skywalker v1"
- board text added: "Flash RSET"
- board text added: "GND"
- board text added: "GPIO Breakout"
- board text added: "GPS 1PPS"
- board text added: "GPS Coaxial"
- board text added: "GPS Coaxial Line Matching Target: 50 ohms Trace width: 0.3424 (Chose JLCPCB Thumbs Up Board for Impedance Calcs)"
- board text added: "I2C0 Debug"
- board text added: "I2C1 Debug"
- board text added: "MCU RSET"
- board text added: "Made with JLCPCB :)"
- board text added: "Module 1 Vout"
- board text added: "Module 2 Vout"
- board text added: "PROVES FC"
- board text added: "RADFET Module 1"
- board text added: "RADFET Module 2"
- board text added: "Reference Layout for Watchdog Circuit! (see OreSat C3 board)"
- board text added: "SWDs & RSet Debug"
- board text added: "Solder to enable Watchdog ---->"
- board text added: "TO DO: - Create BOM - triple check everything to make sure it all works"
- board text added: "Thank you Bouni for making the BOM making process less painful!"
- board text added: "UART0 Debug"
- board text added: "UART1 Debug"
- board text added: "USB Debug"
- board text added: "USB Impedance Matching Target: 90 ohms Trace width: 0.2672mm Trace gap: 0.2032mm (Chose JLCPCB Thumbs Up Board for Impedance Calcs)"
- board text added: "Want Module Vo as close as possible to ADC pins on RP2350 to reduce voltage drops (0.81mV = 1 rad)"
- board text added: "{dblquote}You were the chosen one! It was said that you would destroy the Sith, not join them! Bring balance to the Force, not leave it in darkness!{dblquote}"
